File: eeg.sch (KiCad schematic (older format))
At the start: 150 parts, among them J1 USB_B_Mini, U1 STM32F446RE, U10 -.+2.5V.+3.3V-GND, U11 +5V, U12 RN4678-V_RM100, U13 ADS1299IPAG, U2 ADS1299-8CHANNEL, U3 LD39050PU33R, U4 TPS60403DBVT, U5 TPS73225DBVT, U6 TPS72325DBVT, U61 Electrode2, U7 DATA, U8 Electrode1, U9 ADC_REFGND_GPIO, Y1 16.00Mhz

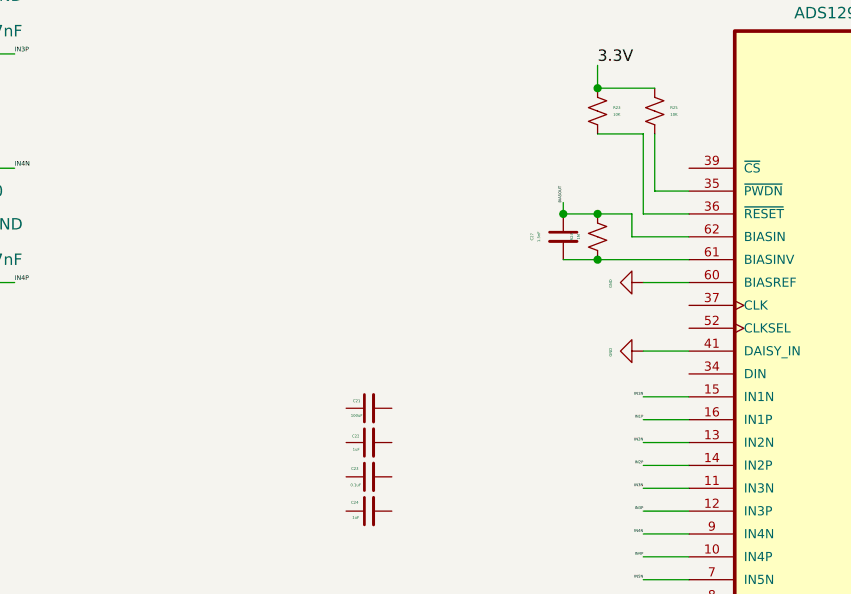
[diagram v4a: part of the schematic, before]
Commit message: Footprints edited and aligned
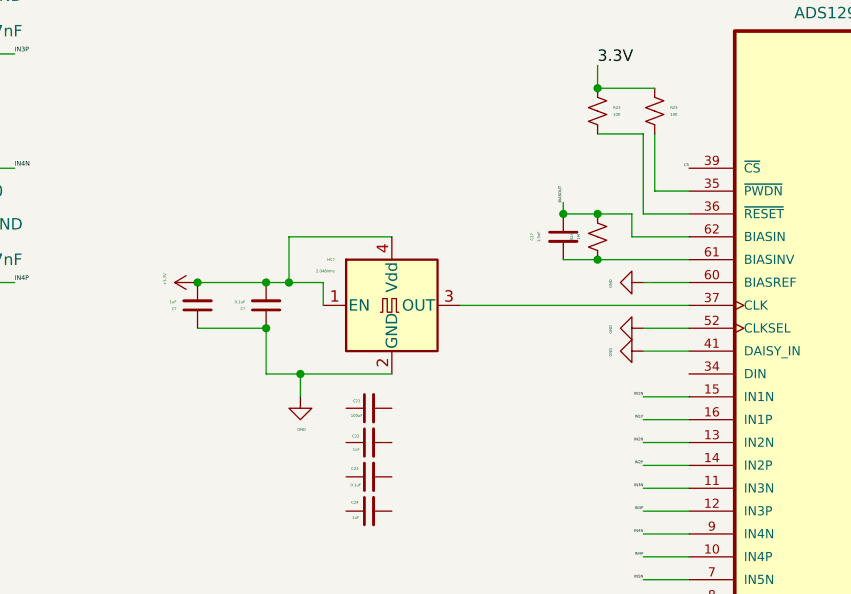
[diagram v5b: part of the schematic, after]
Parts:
- added C?: 0.1uF, Capacitor_SMD:C_0603_1608Metric, symbol Device:C_Small
- added C?: 1uF, Capacitor_SMD:C_0603_1608Metric, symbol Device:C_Small
- added HC?: 2.048mhz, ERA-3A:OSCCC500X320X150N, symbol Oscillator:ASE-xxxMHz
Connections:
- net +3V3: now also C?.2, C?.2, HC?.1 (EN), HC?.4 (Vdd)
- net CS: now also U13.39 (~CS)
- net GND: now also U13.52 (CLKSEL), C?.1, C?.1, HC?.2 (GND)
- net at U13.37 (CLK): now also HC?.3 (OUT)
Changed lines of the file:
@@
 	0    1    1    0
 $EndComp
+Text Label 6650 11100 2    12   ~ 0
+CS
+$Comp
+L power:GND #PWR?
+U 1 1 5FE99C31
+P 6450 11800
+F 0 "#PWR?" H 6450 11550 50  0001 C CNN
+F 1 "GND" H 6455 11657 12  0000 C CNN
+F 2 "" H 6450 11800 50  0001 C CNN
+F 3 "" H 6450 11800 50  0001 C CNN
+	1    6450 11800
+	0    1    1    0
+$EndComp
+Wire Wire Line
+	6450 11800 6650 11800
+$Comp
+L Oscillator:ASE-xxxMHz HC?
+U 1 1 5FEEF50E
+P 5350 11700
+F 0 "HC?" H 5100 11900 12  0000 R CNN
+F 1 "2.048mhz" H 5100 11850 12  0000 R CNN
+F 2 "ERA-3A:OSCCC500X320X150N" H 6050 11350 50  0001 C CNN
+F 3 "http://www.abracon.com/Oscillators/ASV.pdf" H 5250 11700 50  0001 C CNN
+	1    5350 11700
+	1    0    0    -1
+$EndComp
+Wire Wire Line
+	5650 11700 6650 11700
+$Comp
+L Device:C_Small C?
+U 1 1 5FF4A0E4
+P 4800 11700
+F 0 "C?" H 4892 11715 12  0000 L CNN
+F 1 "0.1uF" H 4892 11685 12  0000 L CNN
+F 2 "Capacitor_SMD:C_0603_1608Metric" H 4800 11700 50  0001 C CNN
+F 3 "~" H 4800 11700 50  0001 C CNN
+	1    4800 11700
+	-1   0    0    1
+$EndComp
+$Comp
+L Device:C_Small C?
+U 1 1 5FF53C34
+P 4500 11700
+F 0 "C?" H 4592 11715 12  0000 L CNN
+F 1 "1uF" H 4592 11685 12  0000 L CNN
+F 2 "Capacitor_SMD:C_0603_1608Metric" H 4500 11700 50  0001 C CNN
+F 3 "~" H 4500 11700 50  0001 C CNN
+	1    4500 11700
+	-1   0    0    1
+$EndComp
+Wire Wire Line
+	4950 12000 4950 12100
+Connection ~ 4950 12000
+Wire Wire Line
+	4950 12000 5350 12000
+$Comp
+L power:GND #PWR?
+U 1 1 600C0536
+P 4950 12100
+F 0 "#PWR?" H 4950 11850 50  0001 C CNN
+F 1 "GND" H 4955 11957 12  0000 C CNN
+F 2 "" H 4950 12100 50  0001 C CNN
+F 3 "" H 4950 12100 50  0001 C CNN
+	1    4950 12100
+	1    0    0    -1
+$EndComp
+Wire Wire Line
+	5050 11700 5050 11600
+Wire Wire Line
+	5050 11600 4900 11600
+Connection ~ 4800 11600
+Wire Wire Line
+	4800 11600 4500 11600
+Wire Wire Line
+	4500 11800 4800 11800
+Wire Wire Line
+	4800 11800 4800 12000
+Connection ~ 4800 11800
+Wire Wire Line
+	4800 12000 4950 12000
+$Comp
+L power:+3.3V #PWR?
+U 1 1 601A0CF6
+P 4500 11600
+F 0 "#PWR?" H 4500 11450 50  0001 C CNN
+F 1 "+3.3V" H 4515 11743 12  0000 C CNN
+F 2 "" H 4500 11600 50  0001 C CNN
+F 3 "" H 4500 11600 50  0001 C CNN
+	1    4500 11600
+	0    -1   -1   0
+$EndComp
+Connection ~ 4500 11600
+Wire Wire Line
+	4900 11600 4900 11400
+Wire Wire Line
+	4900 11400 5350 11400
+Connection ~ 4900 11600
+Wire Wire Line
+	4900 11600 4800 11600
 $EndSCHEMATC

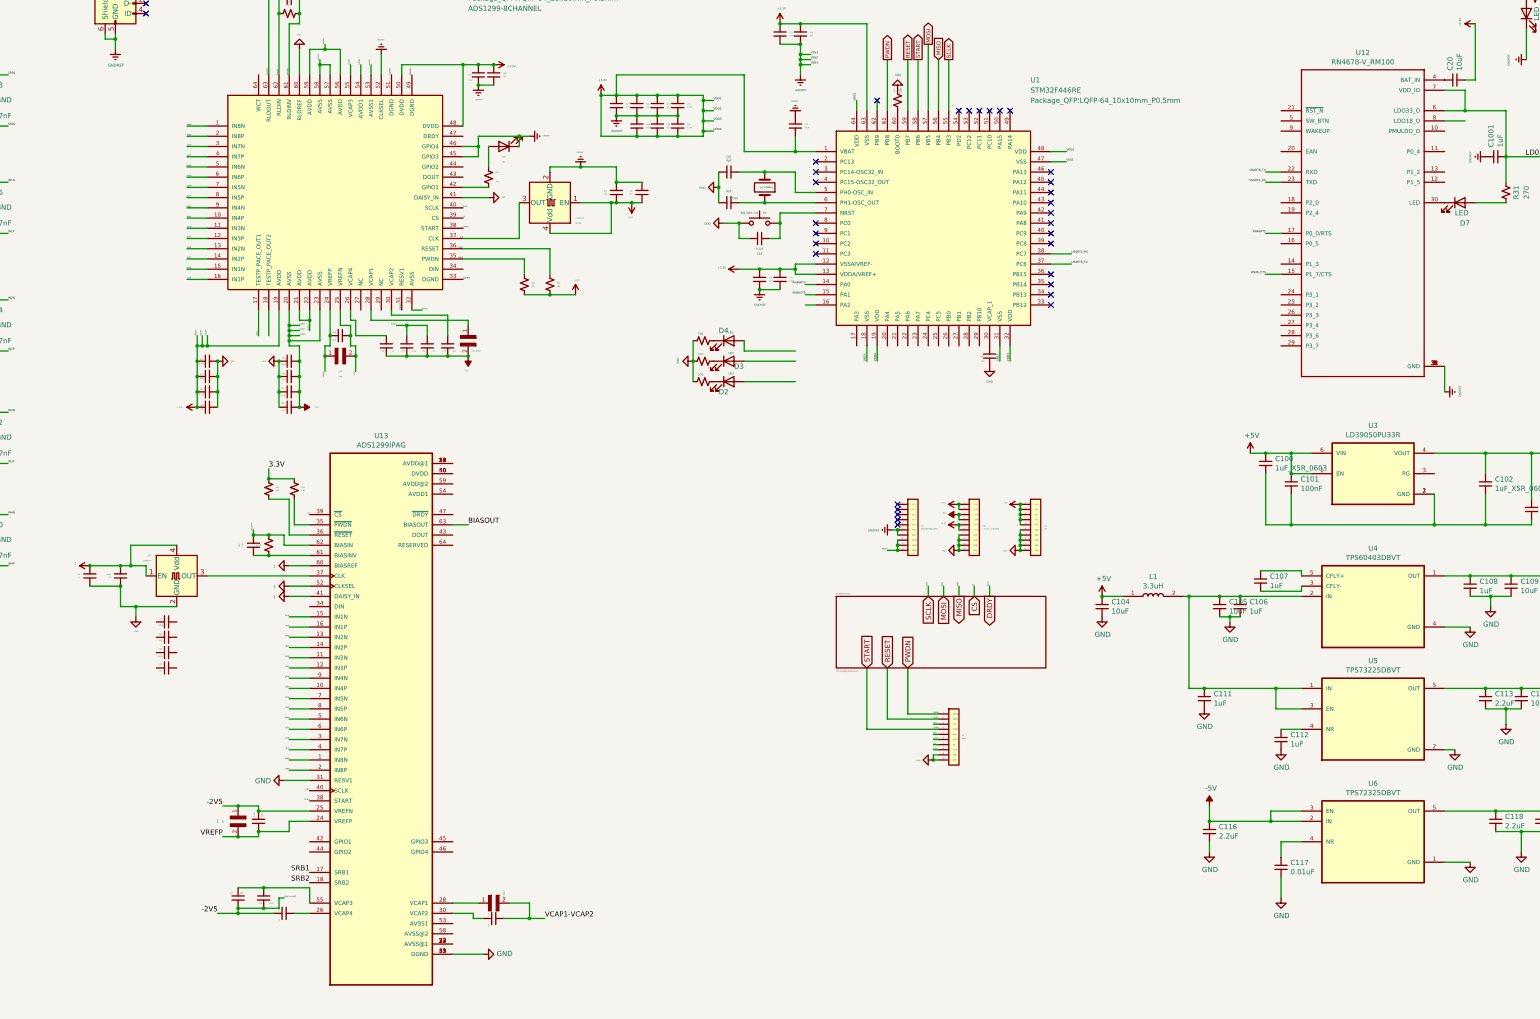
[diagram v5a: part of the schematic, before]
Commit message: Added no connection flags
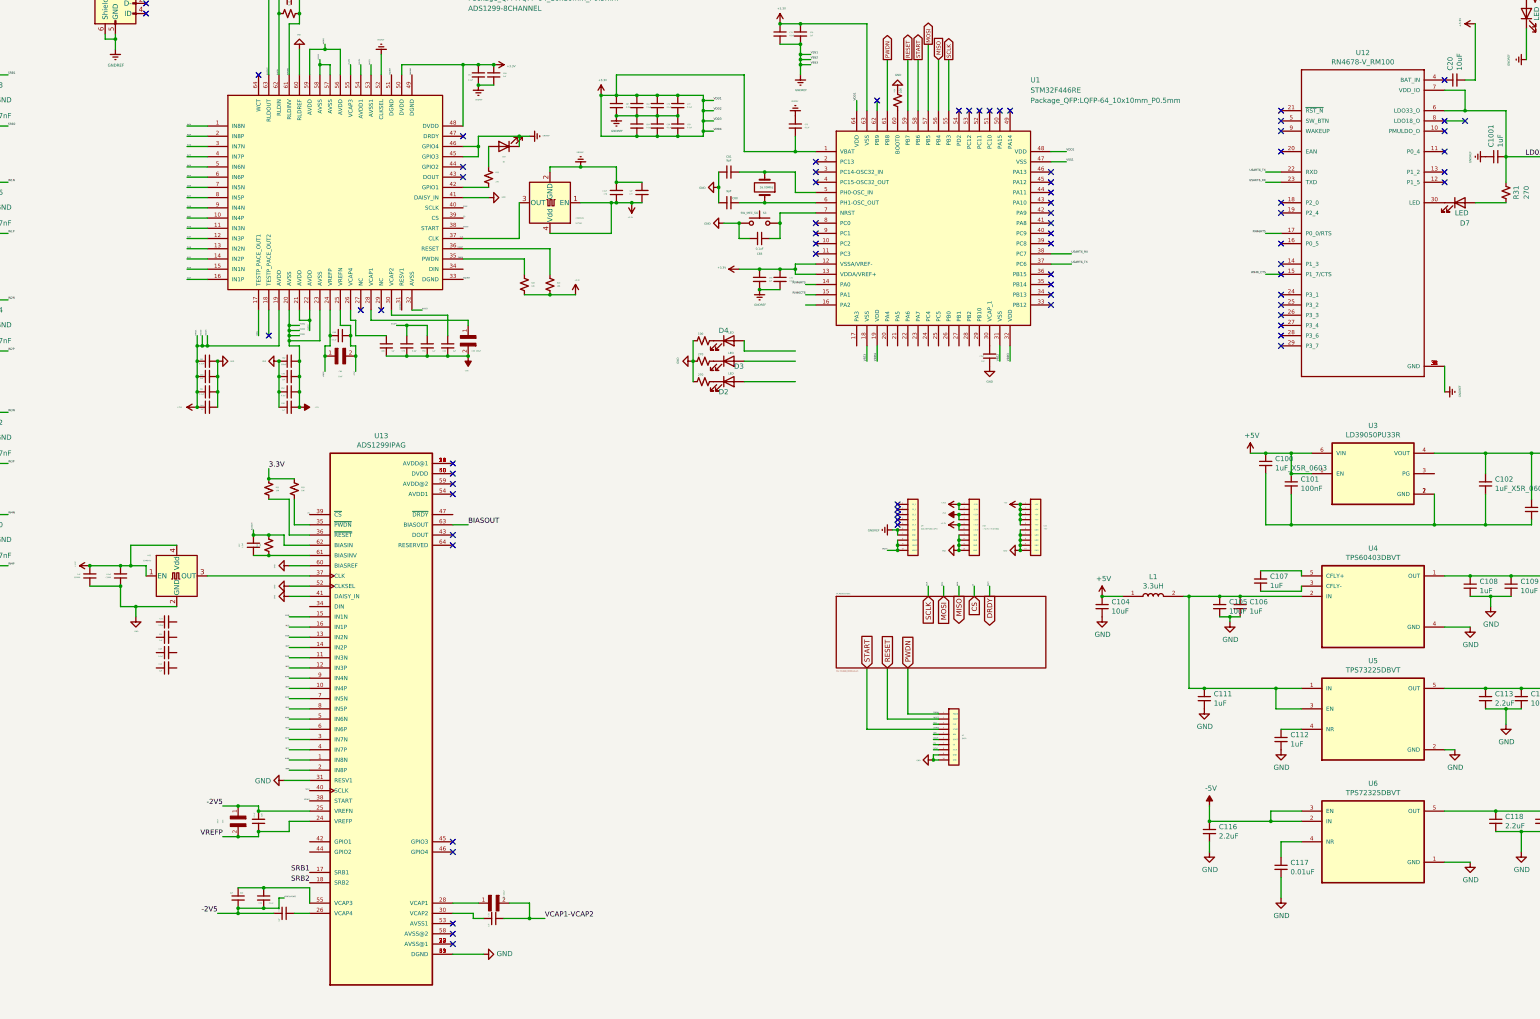
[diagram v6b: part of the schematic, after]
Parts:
- gave numbers to parts that had none: 3
- renumbered HC736 to HC7361
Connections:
- no-connect marks 34 -> 74
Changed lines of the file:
@@
 $EndComp
 $Comp
-L Oscillator:ASE-xxxMHz HC736
+L Oscillator:ASE-xxxMHz HC7361
 U 1 1 5F6C519A
 P 9000 8050
-F 0 "HC736" H 8750 8250 12  0000 R CNN
+F 0 "HC7361" H 8750 8250 12  0000 R CNN
 F 1 "2.048mhz" H 8750 8200 12  0000 R CNN
 F 2 "ERA-3A:OSCCC500X320X150N" H 9700 7700 50  0001 C CNN
@@
 CS
 $Comp
-L power:GND #PWR?
+L power:GND #PWR0133
 U 1 1 5FE99C31
 P 6450 11800
-F 0 "#PWR?" H 6450 11550 50  0001 C CNN
+F 0 "#PWR0133" H 6450 11550 50  0001 C CNN
 F 1 "GND" H 6455 11657 12  0000 C CNN
 F 2 "" H 6450 11800 50  0001 C CNN
@@
 	6450 11800 6650 11800
 $Comp
-L Oscillator:ASE-xxxMHz HC?
+L Oscillator:ASE-xxxMHz HC2
 U 1 1 5FEEF50E
 P 5350 11700
-F 0 "HC?" H 5100 11900 12  0000 R CNN
+F 0 "HC2" H 5100 11900 12  0000 R CNN
 F 1 "2.048mhz" H 5100 11850 12  0000 R CNN
 F 2 "ERA-3A:OSCCC500X320X150N" H 6050 11350 50  0001 C CNN
@@
 	5650 11700 6650 11700
 $Comp
-L Device:C_Small C?
+L Device:C_Small C1000
 U 1 1 5FF4A0E4
 P 4800 11700
-F 0 "C?" H 4892 11715 12  0000 L CNN
+F 0 "C1000" H 4892 11715 12  0000 L CNN
 F 1 "0.1uF" H 4892 11685 12  0000 L CNN
 F 2 "Capacitor_SMD:C_0603_1608Metric" H 4800 11700 50  0001 C CNN
@@
 $EndComp
 $Comp
-L Device:C_Small C?
+L Device:C_Small C10001
 U 1 1 5FF53C34
 P 4500 11700
-F 0 "C?" H 4592 11715 12  0000 L CNN
+F 0 "C10001" H 4592 11715 12  0000 L CNN
 F 1 "1uF" H 4592 11685 12  0000 L CNN
 F 2 "Capacitor_SMD:C_0603_1608Metric" H 4500 11700 50  0001 C CNN
@@
 	4950 12000 5350 12000
 $Comp
-L power:GND #PWR?
+L power:GND #PWR0134
 U 1 1 600C0536
 P 4950 12100
-F 0 "#PWR?" H 4950 11850 50  0001 C CNN
+F 0 "#PWR0134" H 4950 11850 50  0001 C CNN
 F 1 "GND" H 4955 11957 12  0000 C CNN
 F 2 "" H 4950 12100 50  0001 C CNN
@@
 	4800 12000 4950 12000
 $Comp
-L power:+3.3V #PWR?
+L power:+3.3V #PWR0136
 U 1 1 601A0CF6
 P 4500 11600
-F 0 "#PWR?" H 4500 11450 50  0001 C CNN
+F 0 "#PWR0136" H 4500 11450 50  0001 C CNN
 F 1 "+3.3V" H 4515 11743 12  0000 C CNN
 F 2 "" H 4500 11600 50  0001 C CNN
@@
 Wire Wire Line
 	4900 11600 4800 11600
+NoConn ~ 8050 14300
+NoConn ~ 8050 14400
+NoConn ~ 8050 15100
+NoConn ~ 8050 15200
+NoConn ~ 8050 15300
+NoConn ~ 8050 10600
+NoConn ~ 8050 10700
+NoConn ~ 8050 10800
+NoConn ~ 8050 10900
+NoConn ~ 8050 11300
+NoConn ~ 8050 11400
+NoConn ~ 8150 7400
+NoConn ~ 8150 7700
+NoConn ~ 8150 7800
+NoConn ~ 7150 9100
+NoConn ~ 7350 9100
+NoConn ~ 6250 9350
+NoConn ~ 6150 6800
+NoConn ~ 16150 7150
+NoConn ~ 16150 7250
+NoConn ~ 16150 7350
+NoConn ~ 16150 7550
+NoConn ~ 16150 8050
+NoConn ~ 16150 8150
+NoConn ~ 16150 8450
+NoConn ~ 16150 8650
+NoConn ~ 16150 8750
+NoConn ~ 16150 8950
+NoConn ~ 16150 9050
+NoConn ~ 16150 9150
+NoConn ~ 16150 9250
+NoConn ~ 16150 9350
+NoConn ~ 16150 9450
+NoConn ~ 17750 7850
+NoConn ~ 17750 7750
+NoConn ~ 17750 7550
+NoConn ~ 17750 7350
+NoConn ~ 17750 7250
+NoConn ~ 17750 6850
+NoConn ~ 17950 7250
 $EndSCHEMATC

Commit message: Electrodes pins are need to change
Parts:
- removed D2, D3, D4, D6: LED, LED_SMD:LED_0603_1608Metric, symbol Device:LED
- removed R20, R21: 270, Resistor_SMD:R_0603_1608Metric_Pad1.05x0.95mm_HandSolder, symbol Device:R_Small_US
- removed R22: 100, Resistor_SMD:R_0603_1608Metric_Pad1.05x0.95mm_HandSolder, symbol Device:R_Small_US
- removed R30: 100K, Resistor_SMD:R_0603_1608Metric, symbol Device:R_Small_US
- U61: symbol eeg-rescue:Electrode-Electrode-eeg-rescue -> eeg-rescue:Electrode-Electrode-eeg-rescue-eeg-rescue
- U7: symbol eeg-rescue:DATA-Data10Pin -> eeg-rescue:DATA-Data10Pin-eeg-rescue
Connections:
- no-connect marks 74 -> 82
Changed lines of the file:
@@
 Wire Wire Line
 	10650 7900 10650 8050
-$Comp
-L Device:LED D4
-U 1 1 5F59F5DC
-P 10750 9400
-F 0 "D4" H 10650 9500 50  0000 L CNN
-F 1 "LED" H 10743 9480 20  0000 L CNN
-F 2 "LED_SMD:LED_0603_1608Metric" H 10750 9400 50  0001 C CNN
-F 3 "~" H 10750 9400 50  0001 C CNN
-	1    10750 9400
-	1    0    0    -1
-$EndComp
-Wire Wire Line
-	10900 9500 10900 9400
-$Comp
-L Device:R_Small_US R21
-U 1 1 5F5AE843
-P 10500 9600
-F 0 "R21" H 10568 9646 50  0001 L CNN
-F 1 "270" V 10568 9600 20  0000 L CNN
-F 2 "Resistor_SMD:R_0603_1608Metric_Pad1.05x0.95mm_HandSolder" H 10500 9600 50  0001 C CNN
-F 3 "~" H 10500 9600 50  0001 C CNN
-	1    10500 9600
-	0    -1   -1   0
-$EndComp
-$Comp
-L Device:R_Small_US R22
-U 1 1 5F5AEC89
-P 10500 9400
-F 0 "R22" H 10568 9446 50  0001 L CNN
-F 1 "100" V 10568 9400 20  0000 L CNN
-F 2 "Resistor_SMD:R_0603_1608Metric_Pad1.05x0.95mm_HandSolder" H 10500 9400 50  0001 C CNN
-F 3 "~" H 10500 9400 50  0001 C CNN
-	1    10500 9400
-	0    -1   -1   0
-$EndComp
-$Comp
-L power:GND #PWR0114
-U 1 1 5F5B09CA
-P 10400 9600
-F 0 "#PWR0114" H 10400 9350 50  0001 C CNN
-F 1 "GND" H 10405 9451 20  0000 C CNN
-F 2 "" H 10400 9600 50  0001 C CNN
-F 3 "" H 10400 9600 50  0001 C CNN
-	1    10400 9600
-	0    1    -1   0
-$EndComp
-Wire Wire Line
-	10400 9400 10400 9600
-Connection ~ 10400 9600
 Wire Wire Line
 	11250 8150 11250 8250
@@
 Wire Wire Line
 	11250 8150 11600 8150
-Wire Wire Line
-	10900 9600 11400 9600
-Wire Wire Line
-	10900 9500 11400 9500
 $Comp
 L Device:C_Small C42
@@
 $EndComp
 Wire Wire Line
-	10400 9600 10400 9800
-$Comp
-L Device:R_Small_US R20
-U 1 1 5F5AE0AB
-P 10500 9800
-F 0 "R20" H 10568 9846 50  0001 L CNN
-F 1 "270" V 10568 9800 20  0000 L CNN
-F 2 "Resistor_SMD:R_0603_1608Metric_Pad1.05x0.95mm_HandSolder" H 10500 9800 50  0001 C CNN
-F 3 "~" H 10500 9800 50  0001 C CNN
-	1    10500 9800
-	0    -1   -1   0
-$EndComp
-Wire Wire Line
-	10900 9800 11400 9800
-$Comp
-L Device:LED D2
-U 1 1 5F59E7AA
-P 10750 9800
-F 0 "D2" H 10650 9700 50  0000 L CNN
-F 1 "LED" H 10743 9880 20  0000 L CNN
-F 2 "LED_SMD:LED_0603_1608Metric" H 10750 9800 50  0001 C CNN
-F 3 "~" H 10750 9800 50  0001 C CNN
-	1    10750 9800
-	1    0    0    -1
-$EndComp
-Wire Wire Line
 	12200 7150 12200 7050
 $Comp
@@
 $EndComp
 $Comp
-L eeg-rescue:DATA-Data10Pin U7
+L eeg-rescue:DATA-Data10Pin-eeg-rescue U7
 U 1 1 5F52455B
 P 13050 13000
@@
 	0    -1   -1   0
 $EndComp
-$Comp
-L Device:LED D6
-U 1 1 5F5A5A1B
-P 18550 6200
-F 0 "D6" H 18550 6000 50  0000 C CNN
-F 1 "LED" H 18550 6100 50  0000 C CNN
-F 2 "LED_SMD:LED_0603_1608Metric" H 18550 6200 50  0001 C CNN
-F 3 "~" H 18550 6200 50  0001 C CNN
-	1    18550 6200
-	0    -1   -1   0
-$EndComp
-$Comp
-L Device:R_Small_US R30
-U 1 1 5F5AEB9E
-P 18650 6050
-F 0 "R30" H 18450 6200 50  0000 L CNN
-F 1 "100K" H 18400 6100 50  0000 L CNN
-F 2 "Resistor_SMD:R_0603_1608Metric" H 18650 6050 50  0001 C CNN
-F 3 "~" H 18650 6050 50  0001 C CNN
-	1    18650 6050
-	0    1    1    0
-$EndComp
-Wire Wire Line
-	18550 6350 18550 6650
-$Comp
-L power:GNDREF #PWR0177
-U 1 1 5F63B58E
-P 18550 6650
-F 0 "#PWR0177" H 18550 6400 50  0001 C CNN
-F 1 "GNDREF" H 18555 6477 20  0000 C CNN
-F 2 "" H 18550 6650 50  0001 C CNN
-F 3 "" H 18550 6650 50  0001 C CNN
-	1    18550 6650
-	0    1    1    0
-$EndComp
 Wire Wire Line
 	16150 8750 16000 8750
@@
 	18050 6850 17950 6850
 Wire Wire Line
-	18800 6050 18750 6050
-Wire Wire Line
 	17750 7150 17950 7150
 Wire Wire Line
@@
 Wire Wire Line
 	18350 7600 18350 7150
-$Comp
-L Device:LED D3
-U 1 1 5F59ED7C
-P 10750 9600
-F 0 "D3" H 10800 9550 50  0000 L CNN
-F 1 "LED" H 10743 9680 20  0000 L CNN
-F 2 "LED_SMD:LED_0603_1608Metric" H 10750 9600 50  0001 C CNN
-F 3 "~" H 10750 9600 50  0001 C CNN
-	1    10750 9600
-	1    0    0    -1
-$EndComp
 Wire Wire Line
 	2500 12200 2450 12200
@@
 	2450 12300 2500 12300
 $Comp
-L eeg-rescue:Electrode-Electrode-eeg-rescue U61
+L eeg-rescue:Electrode-Electrode-eeg-rescue-eeg-rescue U61
 U 1 1 5F474806
 P 1400 13250
@@
 NoConn ~ 8050 15200
 NoConn ~ 8050 15300
-NoConn ~ 8050 10600
-NoConn ~ 8050 10700
-NoConn ~ 8050 10800
-NoConn ~ 8050 10900
 NoConn ~ 8050 11300
 NoConn ~ 8050 11400
@@
 NoConn ~ 17750 6850
 NoConn ~ 17950 7250
+NoConn ~ 17650 10700
+NoConn ~ 12300 9450
+NoConn ~ 12400 9450
+NoConn ~ 12500 9450
+NoConn ~ 12600 9450
+NoConn ~ 12700 9450
+NoConn ~ 12800 9450
+NoConn ~ 12900 9450
+NoConn ~ 13000 9450
+NoConn ~ 13100 9450
+NoConn ~ 13200 9450
+NoConn ~ 12000 9450
 $EndSCHEMATC

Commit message: Electrode1 and electrode2 schematics are fixed
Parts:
- U61: value Electrode2 -> Electrode1; footprint Connector_PinHeader_1.00mm:PinHeader_2x20_P1.00mm_Vertical -> ADS1299IPAG:openldhardware
- U8: value Electrode1 -> Electrode2; footprint Connector_PinHeader_1.00mm:PinHeader_2x20_P1.00mm_Vertical -> ADS1299IPAG:openldhardware
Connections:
- net RN46_CTS is gone; now on net RN46CTS: U12.15 (P1_7/CTS)
- net +2.5V: now also U61.11 (+2.5V), U61.15 (+2.5V), U61.19 (+2.5V), U61.3 (+2.5V), U61.7 (+2.5V), U8.11 (+2.5V), U8.15 (+2.5V), U8.19 (+2.5V), U8.3 (+2.5V), U8.7 (+2.5V); no longer U61.21 (CSRB2), U61.25 (CIN1P), U61.29 (CIN2P), U61.33 (CIN3P), U61.37 (CIN4P), U8.21 (GND), U8.25 (GND), U8.29 (GND), U8.33 (GND), U8.37 (GND)
- net -2.5V: now also U61.10 (-2.5V), U61.12 (-2.5V), U61.14 (-2.5V), U61.16 (-2.5V), U61.18 (-2.5V), U61.2 (-2.5V), U61.20 (-2.5V), U61.4 (-2.5V), U61.6 (-2.5V), U61.8 (-2.5V), U8.10 (-2.5V), U8.12 (-2.5V), U8.14 (-2.5V), U8.16 (-2.5V), U8.18 (-2.5V), U8.2 (-2.5V), U8.20 (-2.5V), U8.4 (-2.5V), U8.6 (-2.5V), U8.8 (-2.5V); no longer U61.11 (+2.5V), U61.15 (+2.5V), U61.19 (+2.5V), U61.23 (CSRB1), U61.27 (CIN1N), U61.3 (+2.5V), U61.31 (CIN2N), U61.35 (CIN3N), U61.39 (CIN), U61.7 (+2.5V), U8.11 (+2.5V), U8.15 (+2.5V), U8.19 (+2.5V), U8.23 (GND), U8.27 (GND), U8.3 (+2.5V), U8.31 (GND), U8.35 (GND), U8.39 (GND), U8.7 (+2.5V)
- net BIASINV: now also U8.40 (BIASINV); no longer U61.2 (-2.5V)
- net CBIAS: now also U8.38 (CBIAS); no longer U61.6 (-2.5V)
- net CIN1N: now also U61.27 (CIN1N); no longer U8.26 (CIN6P)
- net CIN1P: now also U61.25 (CIN1P); no longer U8.30 (CIN7P)
- net CIN2N: now also U61.31 (CIN2N); no longer U8.18 (-2.5V)
- net CIN2P: now also U61.29 (CIN2P); no longer U8.22 (CIN5P)
- net CIN3N: now also U61.35 (CIN3N); no longer U8.10 (-2.5V)
- net CIN3P: now also U61.33 (CIN3P); no longer U8.14 (-2.5V)
- net CIN4N: now also U61.39 (CIN); no longer U8.2 (-2.5V)
- net CIN4P: now also U61.37 (CIN4P); no longer U8.6 (-2.5V)
- net CIN5N: now also U8.24 (CIN5N); no longer U61.34 (GND)
- net CIN5P: now also U8.22 (CIN5P); no longer U61.38 (GND)
- net CIN6N: now also U8.28 (CIN6N); no longer U61.26 (GND)
- net CIN6P: now also U8.26 (CIN6P); no longer U61.30 (GND)
- net CIN7N: now also U8.32 (CIN7N); no longer U61.18 (-2.5V)
- net CIN7P: now also U8.30 (CIN7P); no longer U61.22 (GND)
- net CIN8N: now also U8.36 (CIN8N); no longer U61.10 (-2.5V)
- net CIN8P: now also U8.34 (CIN8P); no longer U61.14 (-2.5V)
- net CSRB1: now also U61.23 (CSRB1); no longer U8.34 (CIN8P)
- net CSRB2: now also U61.21 (CSRB2); no longer U8.38 (CBIAS)
- net GND: now also C100.2, C101.2, C102.2, C103.2, U3.2 (GND), U3.7 (GND), U61.22 (GND), U61.26 (GND), U61.30 (GND), U61.34 (GND), U61.38 (GND), U8.21 (GND), U8.23 (GND), U8.25 (GND), U8.27 (GND), U8.29 (GND), U8.31 (GND), U8.33 (GND), U8.35 (GND), U8.37 (GND), U8.39 (GND); no longer U61.12 (-2.5V), U61.16 (-2.5V), U61.20 (-2.5V), U61.4 (-2.5V), U61.8 (-2.5V), U8.12 (-2.5V), U8.16 (-2.5V), U8.20 (-2.5V), U8.24 (CIN5N), U8.28 (CIN6N), U8.32 (CIN7N), U8.36 (CIN8N), U8.4 (-2.5V), U8.40 (BIASINV), U8.8 (-2.5V)
